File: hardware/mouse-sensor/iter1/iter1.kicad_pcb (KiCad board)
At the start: 2 copper layers, 22 x 22 mm, 13 parts

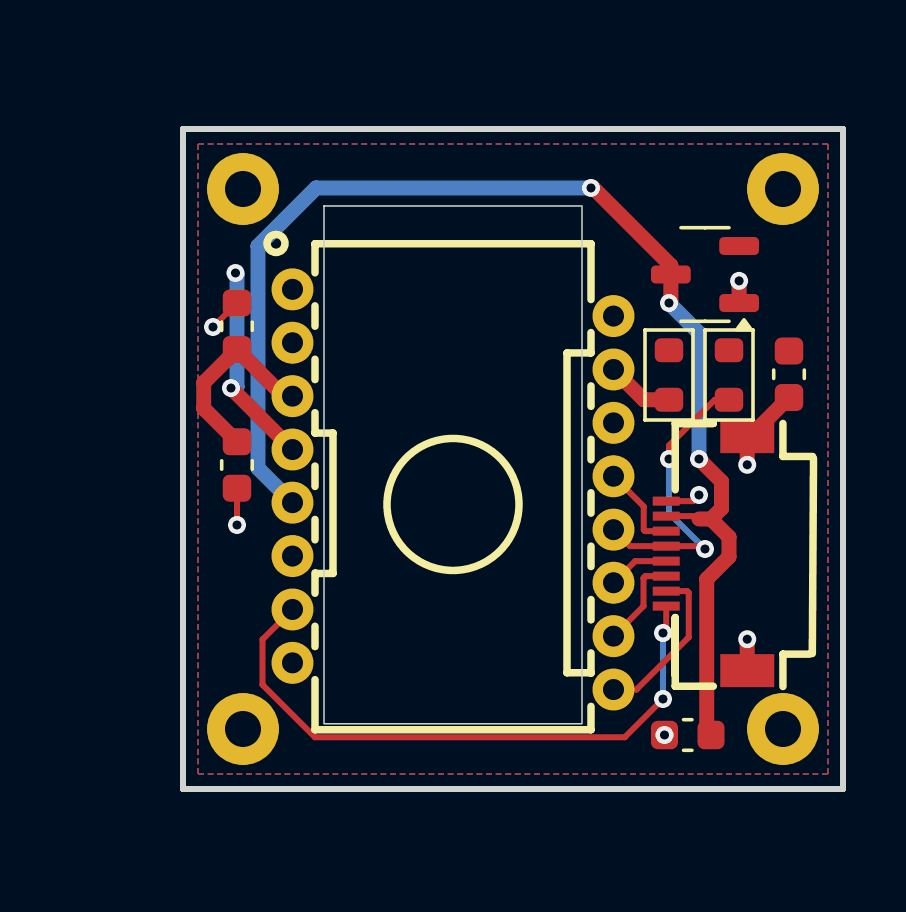
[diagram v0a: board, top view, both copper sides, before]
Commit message: symmetric handsolderable less compact mouse sensor breakout
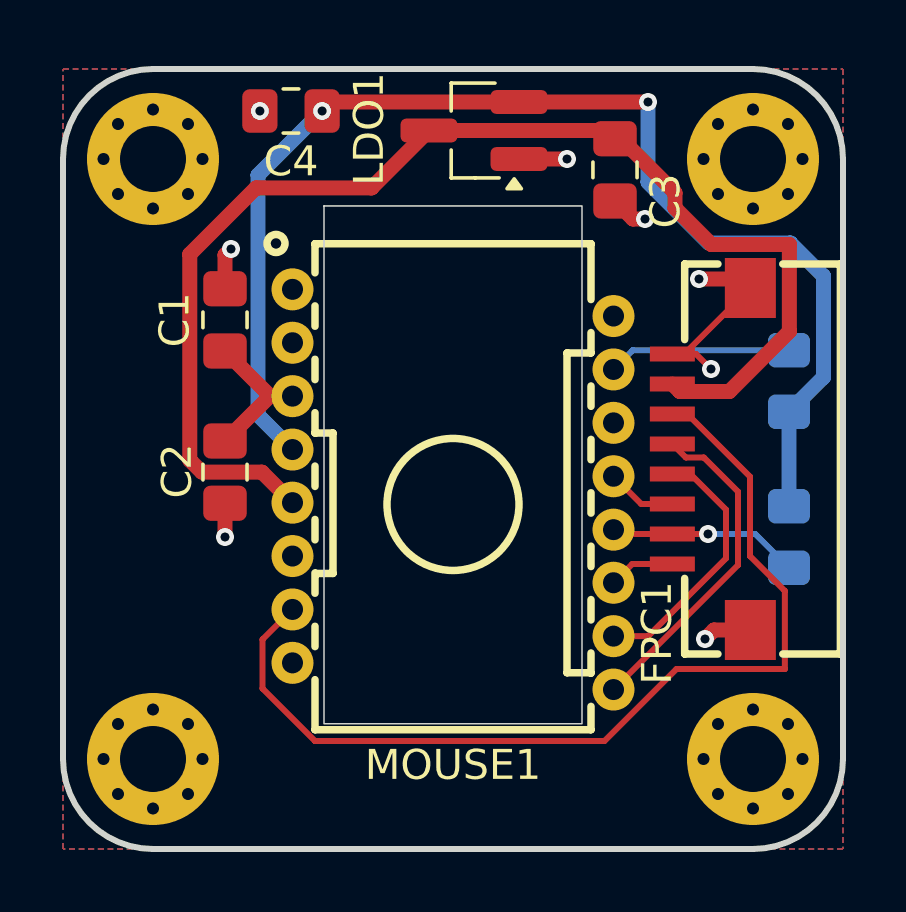
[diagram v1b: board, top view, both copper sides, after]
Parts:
- C1, C2, C3, C4: footprint Capacitor_SMD:C_0603_1608Metric -> Capacitor_SMD:C_0805_2012Metric_Pad1.18x1.45mm_HandSolder
- FPC1: value F0502-B-08-15T-R -> FC10-S08FCT-00; footprint EasyEDA:FPC-SMD_8P-P0.50_F0502-B-08-15T-R -> EasyEDA:FPC-SMD_8P-P1.00_DEALON_FC10-S08FCT-00
- H1, H2, H3, H4: value M1 -> M2; footprint CustomMountingHole:MountingHole_1.2mm_M1_Pad -> MountingHole:MountingHole_2.2mm_M2_Pad_Via
- LDO1: footprint Package_TO_SOT_SMD:SOT-23-3 -> Package_TO_SOT_SMD:SOT-23_Handsoldering
- R1, R2: footprint PCM_Resistor_SMD_AKL:R_0603_1608Metric -> PCM_Resistor_SMD_AKL:R_0805_2012Metric_Pad1.15x1.40mm_HandSolder; moved to B.Cu
- moved C3 19.0 mm to (5.40, -9.64), turned to -90 degrees
- moved C4 18.8 mm to (-5.40, -11.6), turned to 180 degrees
- moved LDO1 9.07 mm to (0.70, -10.9)
- moved R1 5.76 mm to (11.2, 2.60)
- moved R2 4.00 mm to (11.2, -2.60), turned to 90 degrees
- moved H2 3.16 mm to (-10.0, -10.0)
- moved H3 3.16 mm to (-10.0, 10.0)
- moved FPC1 3.16 mm to (8.61, 0.00)
- moved H1 1.41 mm to (10.0, -10.0)
- moved H4 1.41 mm to (10.0, 10.0)
- moved C2 0.47 mm to (-7.60, 0.44)
- moved C1 0.45 mm to (-7.60, -4.64)
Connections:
- FPC1 pad 1: /RST -> /MOSI
- FPC1 pad 2: /MOT -> /MISO
- FPC1 pad 3: /SCLK -> /SCS
- FPC1 pad 4: /MOSI -> /SCLK
- FPC1 pad 5: /MISO -> /MOT
- FPC1 pad 6: /SCS -> /RST
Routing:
- net +1V8: track 6.93 -> 41.6 mm
- net /RST: track 20.7 -> 32.5 mm, vias 2 -> 0
- net /MOT: track 5.49 -> 11.2 mm
- net GND: track 8.21 -> 13.9 mm, vias 7 -> 8
- net /SCLK: track 3.14 -> 8.73 mm
- net Net-(MOUSE1-LED_P): track 2.27 -> 6.12 mm
- net /MISO: track 9.90 -> 6.40 mm, vias 2 -> 1
- net +3V3: track 43.4 -> 42.2 mm, vias 3 -> 0
- net Net-(MOUSE1-VDDPIX): track 6.49 -> 5.74 mm
- net /SCS: track 2.97 -> 2.35 mm
- added copper zone on F.Cu, net +3V3
- removed copper zone on F.Cu, net +1V8
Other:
- board size 22 x 22 mm -> 26 x 26 mm
